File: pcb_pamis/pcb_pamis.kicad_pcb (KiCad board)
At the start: 4 copper layers, 79 x 100.5 mm, 59 parts, among them J1 USB_C_Receptacle_USB2.0_16P, J10 Conn_01x03, J11 Conn_01x03, J12 Conn_02x06_Odd_Even, J2 1755736, J3 Conn_01x04, J4 Conn_01x04, J5 Conn_01x04, J6 Conn_01x05, J7 Conn_01x05, J8 Conn_01x05, J9 Conn_01x03, Q1 Q_NPN_BEC, Q2 Q_NPN_BEC, SW1 SW_Push, U1 ESP32-WROOM-32UE, U2 CP2102N-Axx-xQFN28, U3 TMC2209_SILENTSTEPSTICK, U4 TMC2209_SILENTSTEPSTICK, U5 TMC2209_SILENTSTEPSTICK

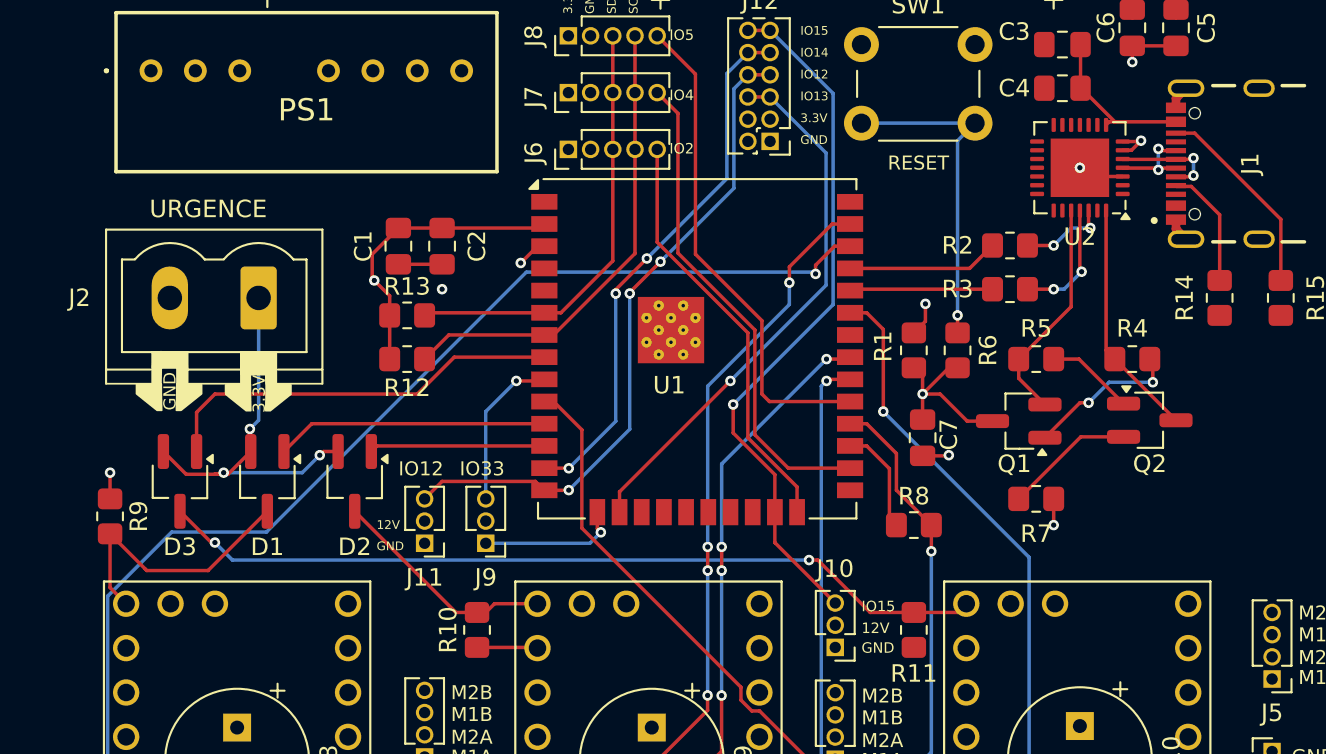
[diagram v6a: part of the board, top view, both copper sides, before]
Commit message: suppression vias GND inutiles + ajout logo modelec
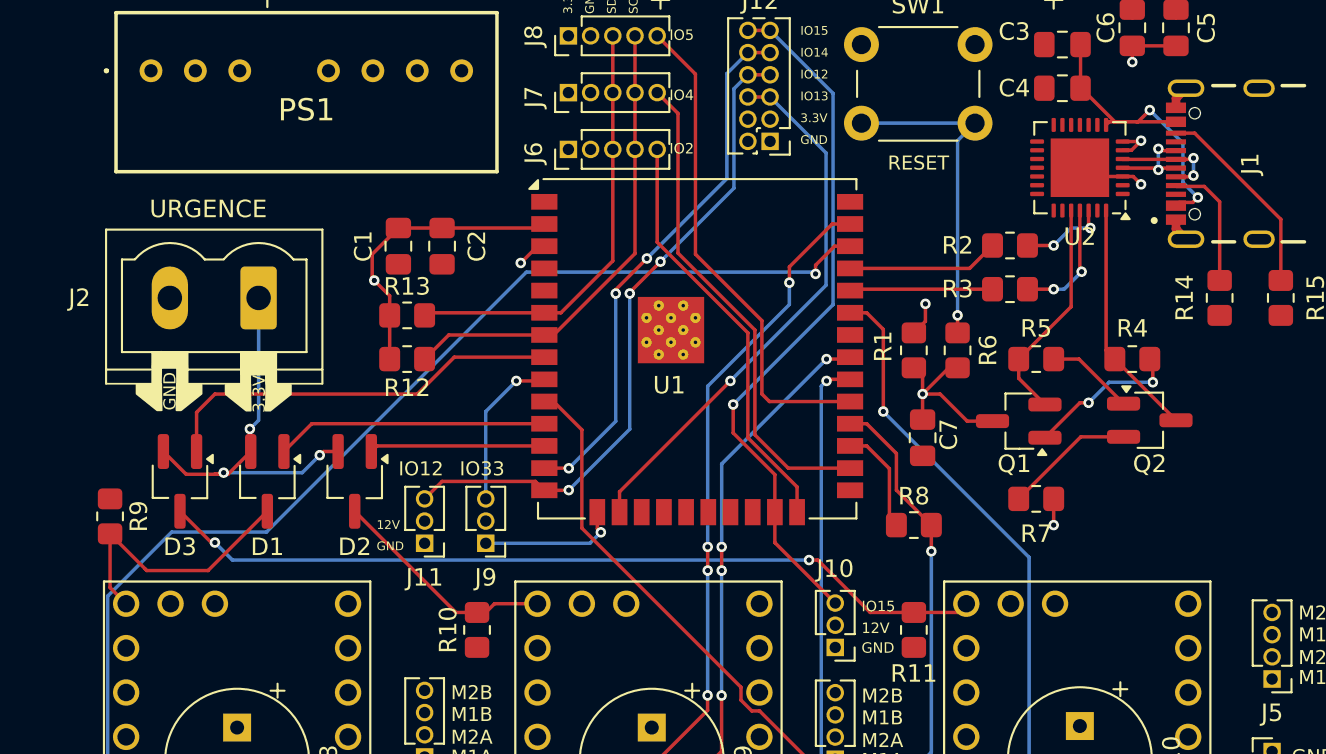
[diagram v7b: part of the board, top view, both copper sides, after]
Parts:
- added G***: LOGO, Modelec:logo_modelec, B.Cu at (108.5, 50.5)
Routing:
- net VBUS: track 9.31 -> 17.9 mm, vias 0 -> 2
- net GND: track 23.5 -> 15.8 mm, vias 5 -> 2
